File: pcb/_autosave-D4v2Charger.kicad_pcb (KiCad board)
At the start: 2 copper layers, 17 x 14 mm, 15 parts, among them J1 Conn_01x02_Pin, U1 BQ25185DLHR

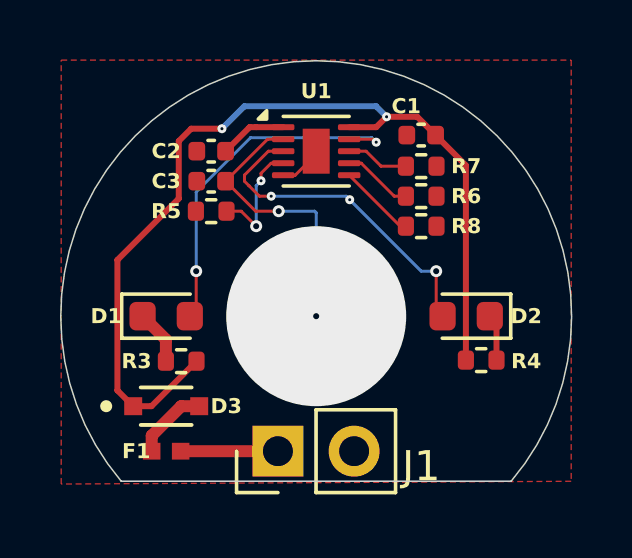
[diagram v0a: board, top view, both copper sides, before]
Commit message: SYS pin fix
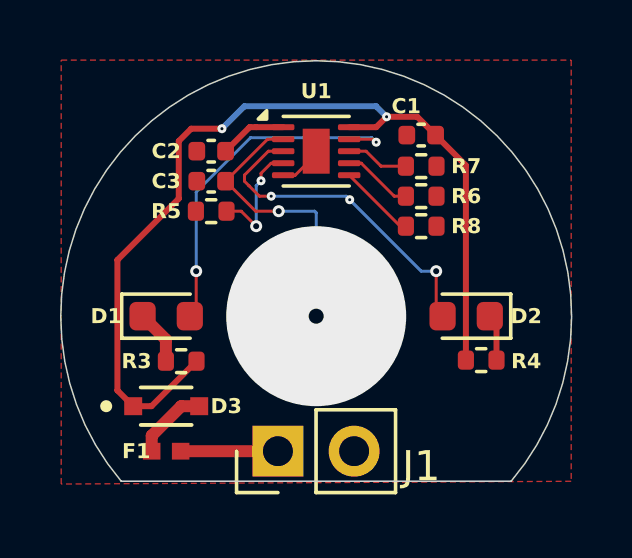
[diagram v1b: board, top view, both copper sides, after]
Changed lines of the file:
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@@
 		(net 6)
 	)
-	(via
+	(via blind
 		(at 143.5 93)
 		(size 6)
-		(drill 0.2)
+		(drill 0.5)
 		(layers "F.Cu" "B.Cu")
+		(tenting none)
 		(net 6)
 	)
